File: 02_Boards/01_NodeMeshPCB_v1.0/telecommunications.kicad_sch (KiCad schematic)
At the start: 0 parts

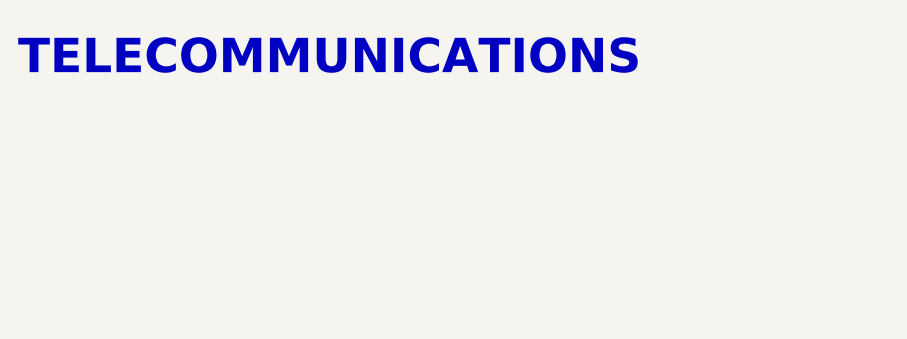
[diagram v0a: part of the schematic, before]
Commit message: 3V3 LDO Schematic
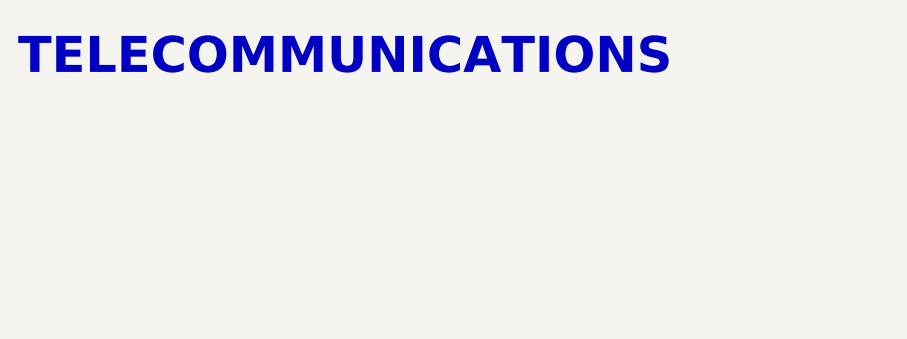
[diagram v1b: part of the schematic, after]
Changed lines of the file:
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@@
 		(effects
 			(font
-				(size 3.81 3.81)
+				(size 4 4)
 				(bold yes)
 			)

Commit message: ht-ra62 schematic
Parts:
- added J3: SMAJPHRATH1, CONN_SMA-J-P-H-RA-TH1_SAI, symbol SMAJPHRATH1:SMA-J-P-H-RA-TH1
- added R9: 0Ohm, symbol Device:R
- added U5: HT-RA62, symbol HT-RA62:HT-RA62
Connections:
- new net: R9.1, U5.5 (TXEN)
- new net: R9.2, U5.7 (DIO2)
- new net: J3.1, U5.1 (ANT)
- new net: J3.2, J3.3, J3.4, J3.5, U5.16 (GND), U5.2 (GND), U5.9 (GND)
- new net LR_BUSY: U5.10 (BUSY)
- new net LR_DIO1: U5.6 (DIO1)
- new net LR_RST: U5.4 (RESET)
- new net LR_RXEN: U5.11 (RXEN)
- new net MISO: U5.13 (MISO)
- new net MOSI: U5.14 (MOSI)
- new net NSS: U5.15 (NSS)
- new net SCK: U5.12 (SCK)
- new net V_SYS: U5.3 (3.3V)
- no-connect marks 0 -> 1
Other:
- note added: "LORA MODULE HT-RA62"

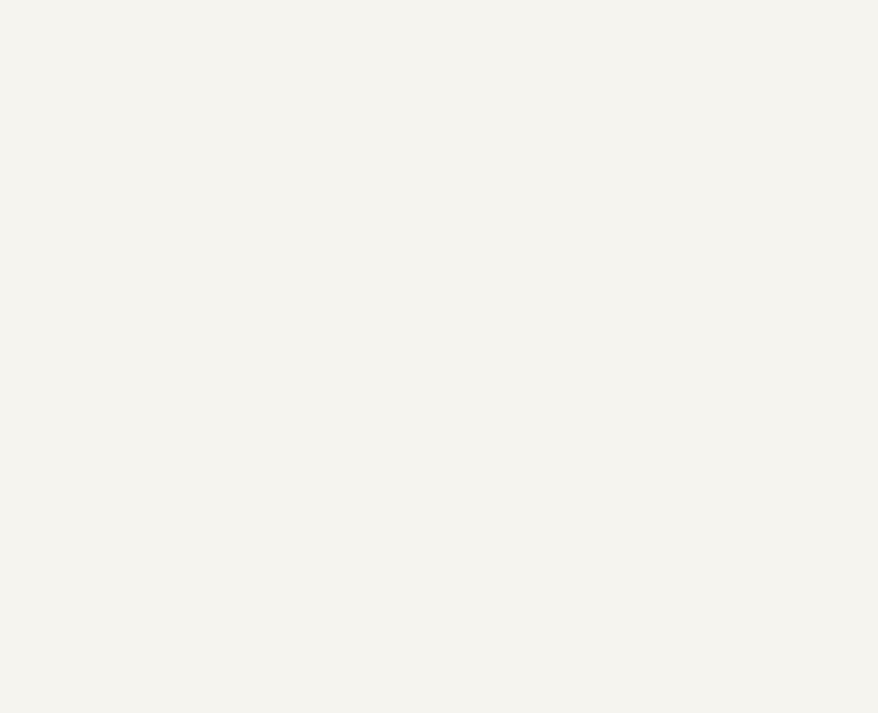
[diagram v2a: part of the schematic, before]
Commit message: firmware project creation
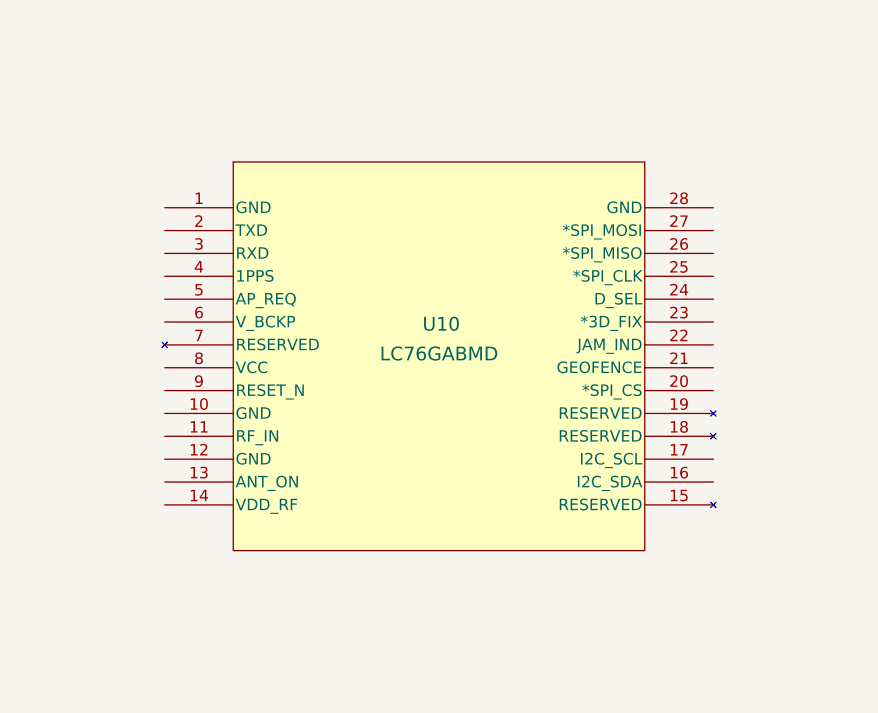
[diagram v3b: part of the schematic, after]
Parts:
- added U10: LC76GABMD, LC76G_QWS, symbol LC76GABMD:LC76GABMD
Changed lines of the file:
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@@
+	)
+	(symbol
+		(lib_id "LC76GABMD:LC76GABMD")
+		(at 173.99 48.26 0)
+		(unit 1)
+		(exclude_from_sim no)
+		(in_bom yes)
+		(on_board yes)
+		(dnp no)
+		(property "Reference" "U10"
+			(at 204.724 61.214 0)
+			(effects
+				(font
+					(size 1.524 1.524)
+				)
+			)
+		)
+		(property "Value" "LC76GABMD"
+			(at 204.47 64.516 0)
+			(effects
+				(font
+					(size 1.524 1.524)
+				)
+			)
+		)
+		(property "Footprint" "LC76G_QWS"
+			(at 173.99 48.26 0)
+			(effects
+				(font
+					(size 1.27 1.27)
+					(italic yes)
+				)
+				(hide yes)
+			)
+		)
+		(property "Datasheet" "LC76GABMD"
+			(at 173.99 48.26 0)
+			(effects
+				(font
+					(size 1.27 1.27)
+					(italic yes)
+				)
+				(hide yes)
+			)
+		)
+		(property "Description" ""
+			(at 173.99 48.26 0)
+			(effects
+				(font
+					(size 1.27 1.27)
+				)
+				(hide yes)
+			)
+		)
+		(pin "1"
+		)
+		(pin "2"
+		)
+		(pin "3"
+		)
+		(pin "4"
+		)
+		(pin "5"
+		)
+		(pin "6"
+		)
+		(pin "7"
+		)
+		(pin "8"
+		)
+		(pin "9"
+		)
+		(pin "10"
+		)
+		(pin "11"
+		)
+		(pin "12"
+		)
+		(pin "13"
+		)
+		(pin "14"
+		)
+		(pin "28"
+		)
+		(pin "27"
+		)
+		(pin "26"
+		)
+		(pin "25"
+		)
+		(pin "24"
+		)
+		(pin "23"
+		)
+		(pin "22"
+		)
+		(pin "21"
+		)
+		(pin "20"
+		)
+		(pin "19"
+		)
+		(pin "18"
+		)
+		(pin "17"
+		)
+		(pin "16"
+		)
+		(pin "15"
+		)
+		(instances
+			(project ""
+				(path "/1ce5abde-bad5-41d0-ae59-b000d0618a73/173837b4-3307-4670-8f9a-15daadfcd562"
+					(reference "U10")
+					(unit 1)
+				)
+			)
+		)
 	)
 	(symbol

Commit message: PCB placement
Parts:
- removed J3: SMAJPHRATH1, CONN_SMA-J-P-H-RA-TH1_SAI, symbol SMAJPHRATH1:SMA-J-P-H-RA-TH1
- added C35: 100pF, Capacitor_SMD:C_0603_1608Metric, symbol Device:C
- added C36, C37, C38: 100nF, Capacitor_SMD:C_0603_1608Metric, symbol Device:C
- added J6, J7: SMA-J-P-H-ST-TH1, 01_Footprints:SMA-J-P-H-ST-TH1, symbol SMA-J-P-H-ST-TH1:SMA-J-P-H-ST-TH1
- added L6: 82nH, Inductor_SMD:L_0603_1608Metric, symbol Device:L
- added R21, R22, R26, R27, R28: 0Ohm, Resistor_SMD:R_0603_1608Metric, symbol Device:R
- added R23: 100kOhm, Resistor_SMD:R_0603_1608Metric, symbol Device:R
- added R24: 1kOhm, Resistor_SMD:R_0603_1608Metric, symbol Device:R
- added SW5: B3U-1000P, Button_Switch_SMD:SW_SPST_B3U-1000P, symbol Switch:SW_Push
- R25: renamed from R9; footprint (none) -> Resistor_SMD:R_0603_1608Metric
- U7: renamed from U5; footprint (none) -> 01_Footprints:HT-RA62
- U8: renamed from U10; footprint LC76G_QWS -> 01_Footprints:LC76GABMD
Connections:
- net GND: now reaches U8.1 (GND)
- net GND: now also U7.16 (GND), U7.2 (GND), U7.9 (GND), U8.10 (GND), U8.12 (GND), U8.28 (GND), C36.2, C37.2, C38.2, J6.G1, J6.G2, J6.G3, J6.G4, J7.G1, J7.G2, J7.G3, J7.G4, R26.2, SW5.2
- net at U8.11 (RF_IN): now also C35.1
- net VDD_RF: now reaches U8.14 (VDD_RF)
- net VDD_RF: now also C37.1, R24.1
- net at U8.16 (I2C_SDA): now also R21.2
- net at U8.17 (I2C_SCL): now also R22.2
- net at U8.2 (TXD): now also R28.1
- net at U8.24 (D_SEL): now also R26.1
- net at U8.3 (RXD): now also R27.1
- net V_GPS: now reaches U8.6 (V_BCKP)
- net V_GPS: now also U8.8 (VCC), R23.2
- net GPS_RESET: now reaches U8.9 (RESET_N)
- net GPS_RESET: now also C38.1, R23.1, SW5.1
- net at U7.1 (ANT): now also J7.1
- new net: C36.1, L6.1, R24.2
- new net: C35.2, J6.1, L6.2
- new net GPS_RX: R28.2
- new net GPS_TX: R27.2
- new net SCL: R22.1
- new net SDA: R21.1
- no-connect marks 1 -> 11
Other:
- note added: "GPS ANTENNA"
- note added: "GPS MODULE QUECTEL LC76ABMD"
- note added: "GPS RESET"
- note added: "LORA ANTENNA"
- moved on the sheet: R25, U7, U8
